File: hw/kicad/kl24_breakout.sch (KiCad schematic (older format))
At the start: 26 parts

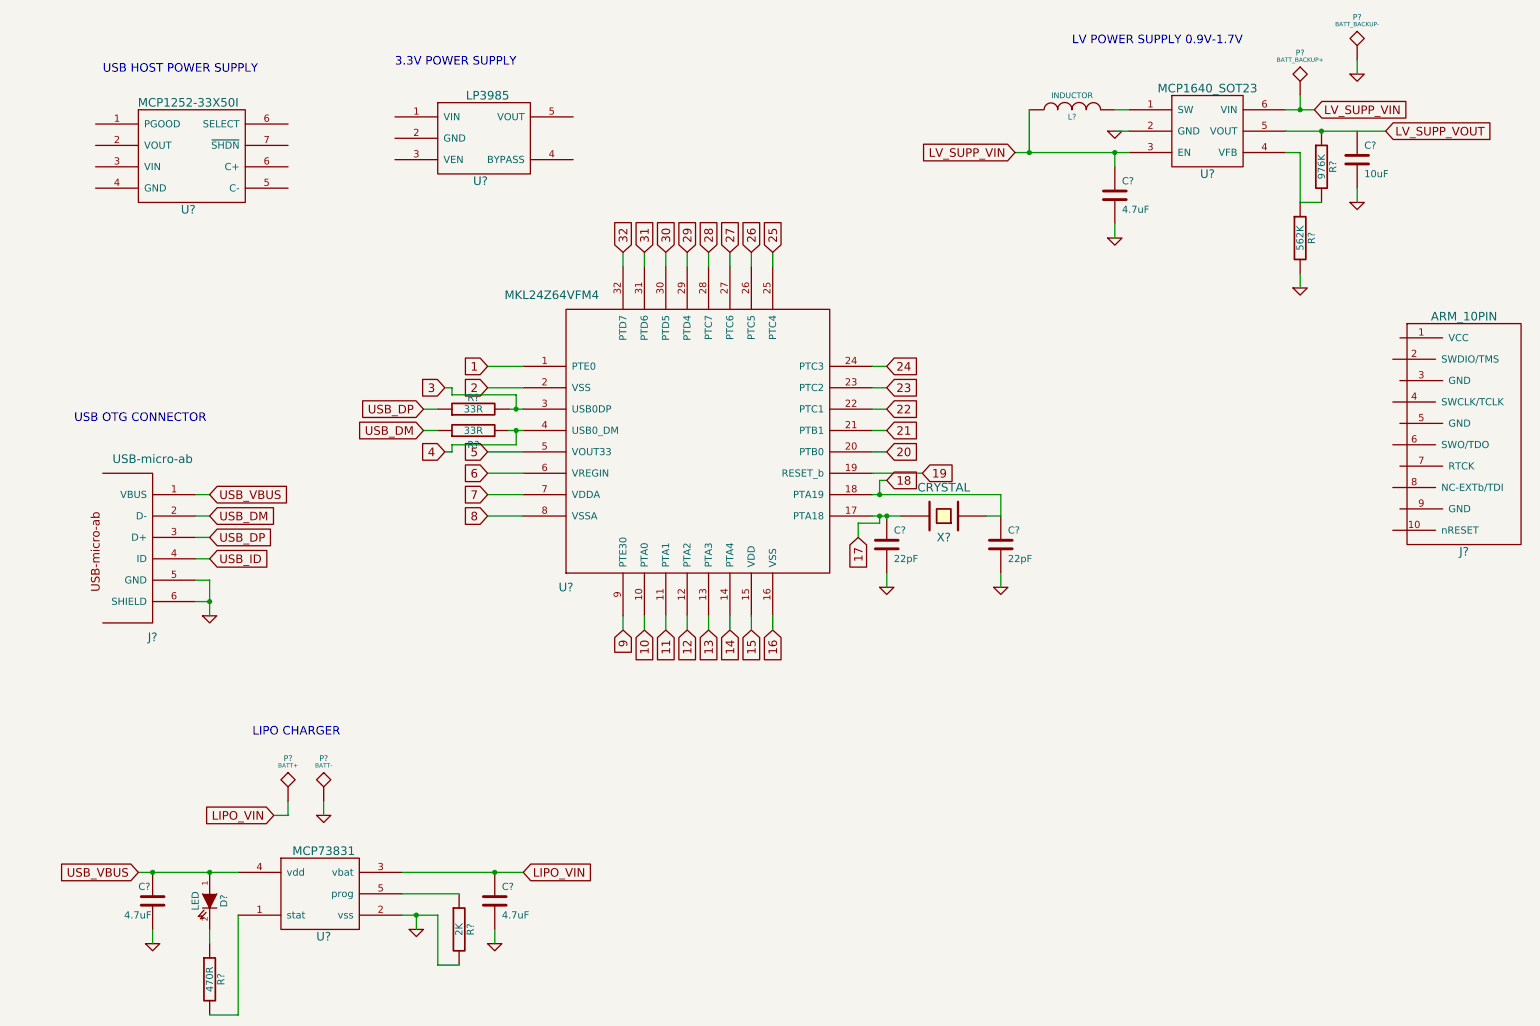
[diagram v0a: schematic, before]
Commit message: - populate 3.3v supply, som rearragning
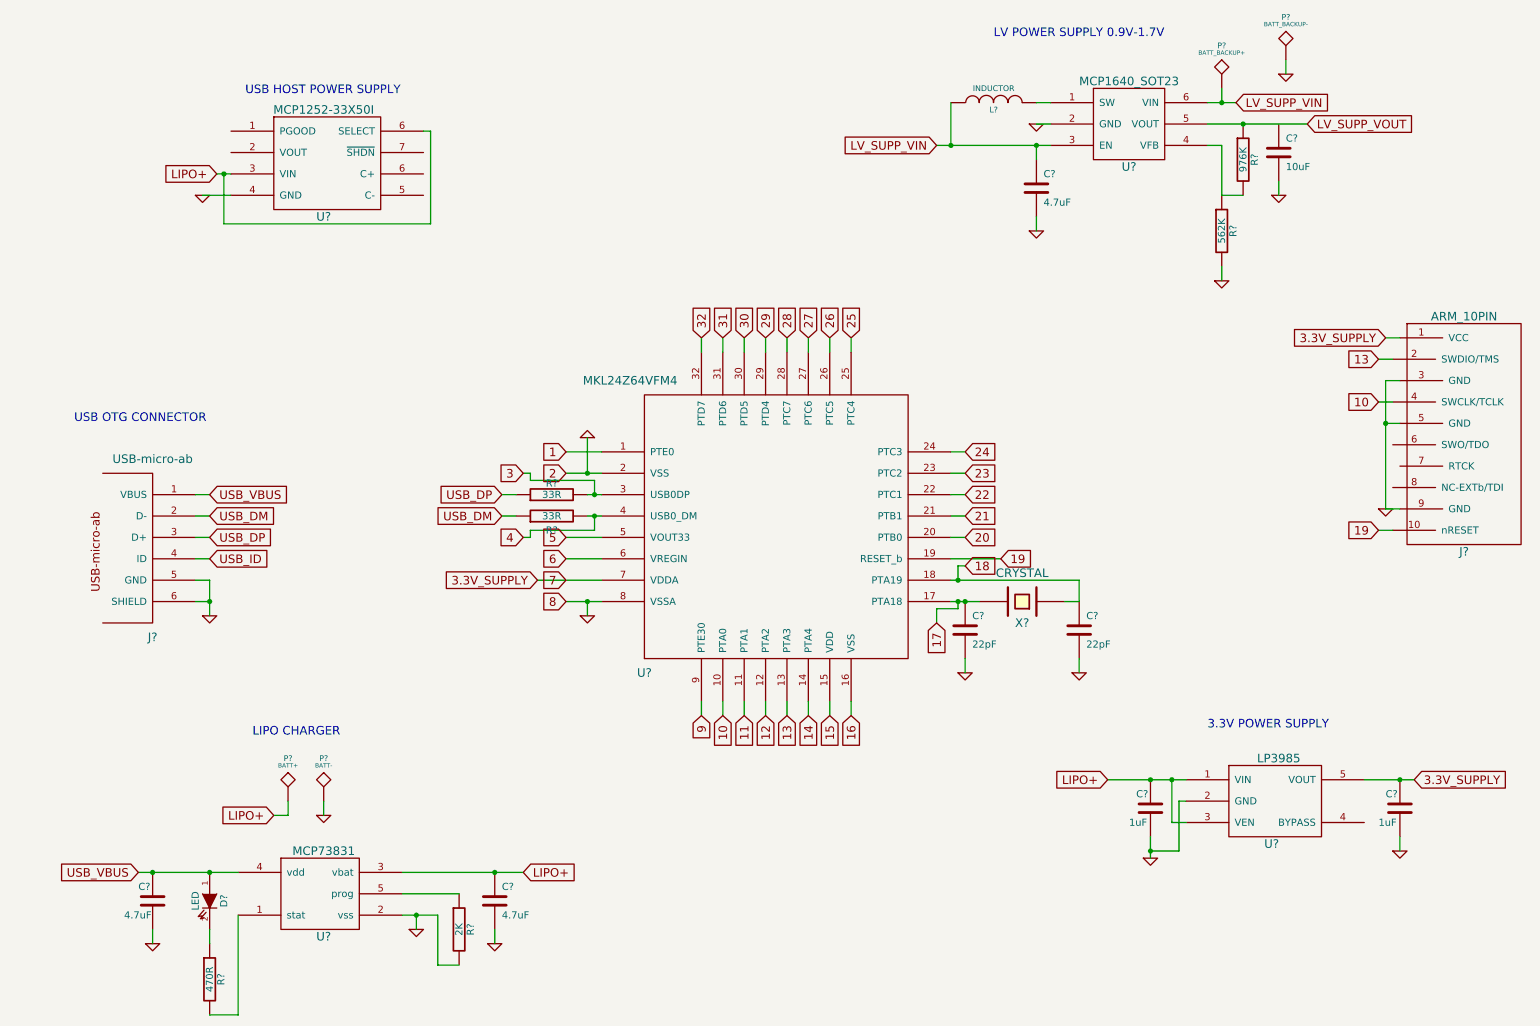
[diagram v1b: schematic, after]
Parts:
- added C? (x2): 1uF, symbol C
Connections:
- net 2 is gone; now on net GND: U?.2 (VSS)
- net 7 is gone; now on net 3.3V_SUPPLY: U?.7 (VDDA)
- net 8 is gone; now on net GND: U?.8 (VSSA)
- net LIPO_VIN is gone; now on net LIPO+: C?.1, P?.1, U?.3 (vbat)
- net 10: now also J?.4 (SWCLK/TCLK)
- net 13: now also J?.2 (SWDIO/TMS)
- net 19: now also J?.10 (nRESET)
- net GND: now also J?.3 (GND), J?.5 (GND), J?.9 (GND), U?.2 (GND), U?.4 (GND), C?.2, C?.2
- net 3.3V_SUPPLY: now reaches J?.1 (VCC)
- net 3.3V_SUPPLY: now also U?.5 (VOUT), C?.1
- net LIPO+: now reaches U?.1 (VIN)
- net LIPO+: now also U?.3 (VEN), U?.3 (VIN), U?.6 (SELECT), C?.1
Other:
- moved on the sheet: C?, L?, P?, R?, U?, X?

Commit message: - fix some erc's - add test points for all micro pins
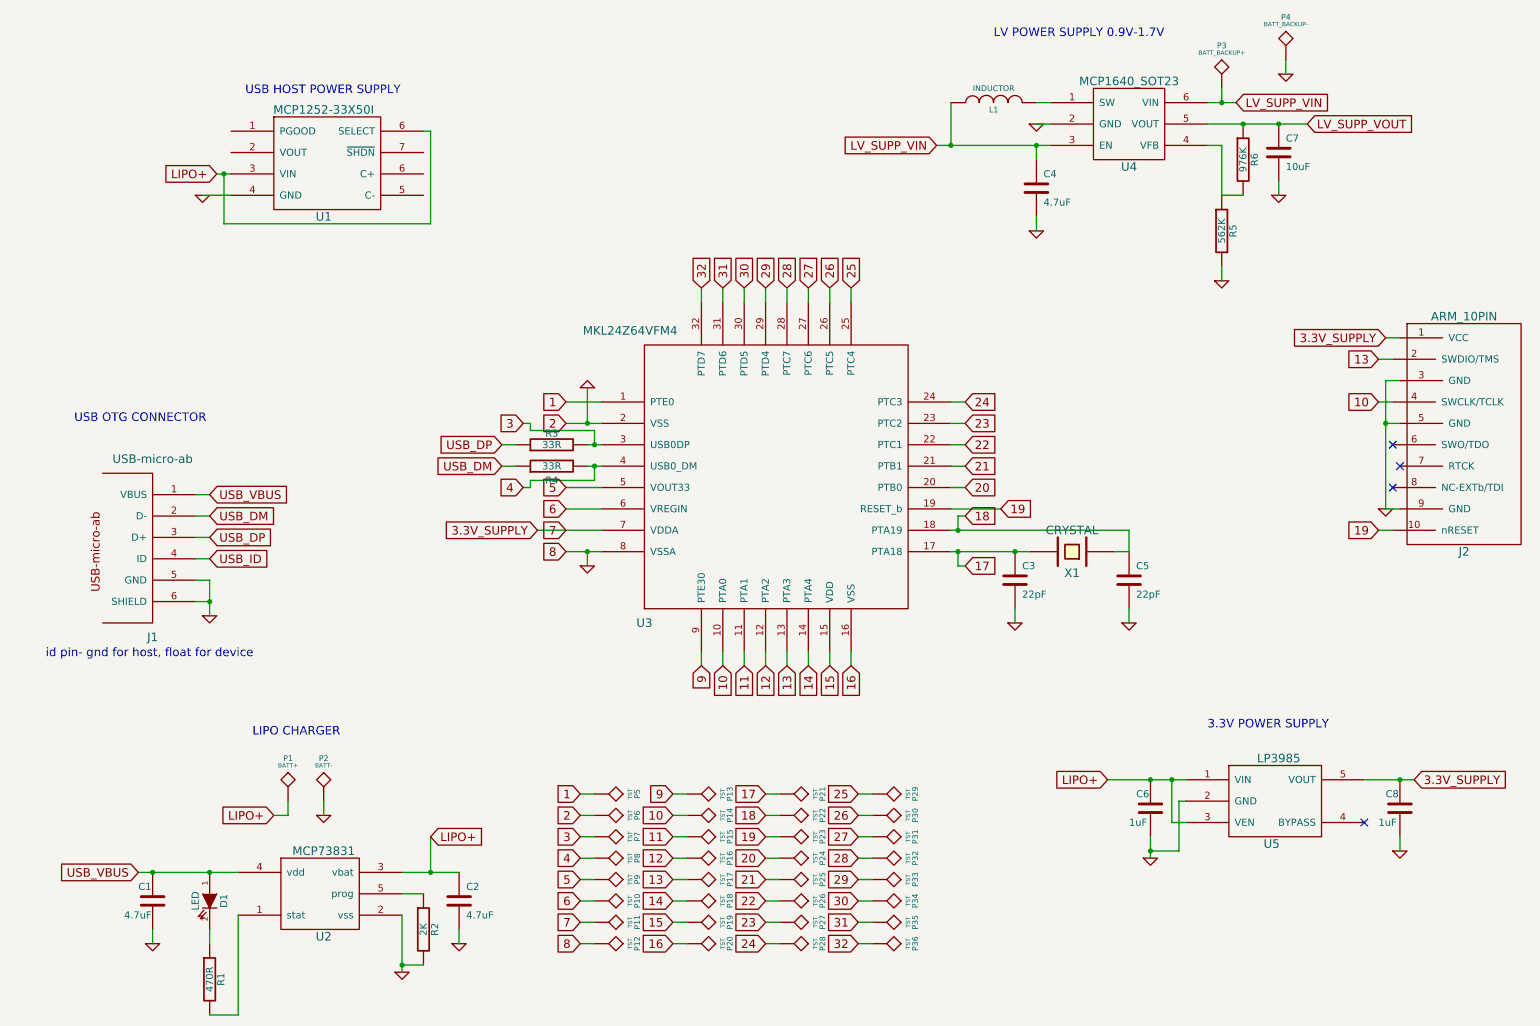
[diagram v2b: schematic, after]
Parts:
- added P10, P11, P12, P13, P14, P15, P16, P17, P18, P19, P20, P21, P22, P23, P24, P25, P26, P27, P28, P29, P30, P31, P32, P33, P34, P35, P36, P5, P6, P7, P8, P9: TST, ~, symbol TST
- gave numbers to parts that had none: 28
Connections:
- net 1: now also P5.1
- net 10: now also P14.1
- net 11: now also P15.1
- net 12: now also P16.1
- net 13: now also P17.1
- net 14: now also P18.1
- net 15: now also P19.1
- net 16: now also P20.1
- net 17: now also P21.1
- net 18: now also P22.1
- net 19: now also P23.1
- net 20: now also P24.1
- net 21: now also P25.1
- net 22: now also P26.1
- net 23: now also P27.1
- net 24: now also P28.1
- net 25: now also P29.1
- net 26: now also P30.1
- net 27: now also P31.1
- net 28: now also P32.1
- net 29: now also P33.1
- net 3: now also P7.1
- net 3.3V_SUPPLY: now also P11.1
- net 30: now also P34.1
- net 31: now also P35.1
- net 32: now also P36.1
- net 4: now also P8.1
- net 5: now also P9.1
- net 6: now also P10.1
- net 9: now also P13.1
- net GND: now also P12.1, P6.1
- net LV_SUPP_VOUT: now also C7.1
- no-connect marks 0 -> 4
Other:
- note added: "id pin- gnd for host, float for device"
- moved on the sheet: C2, C3, C5, R2, R3, R4, U3, X1

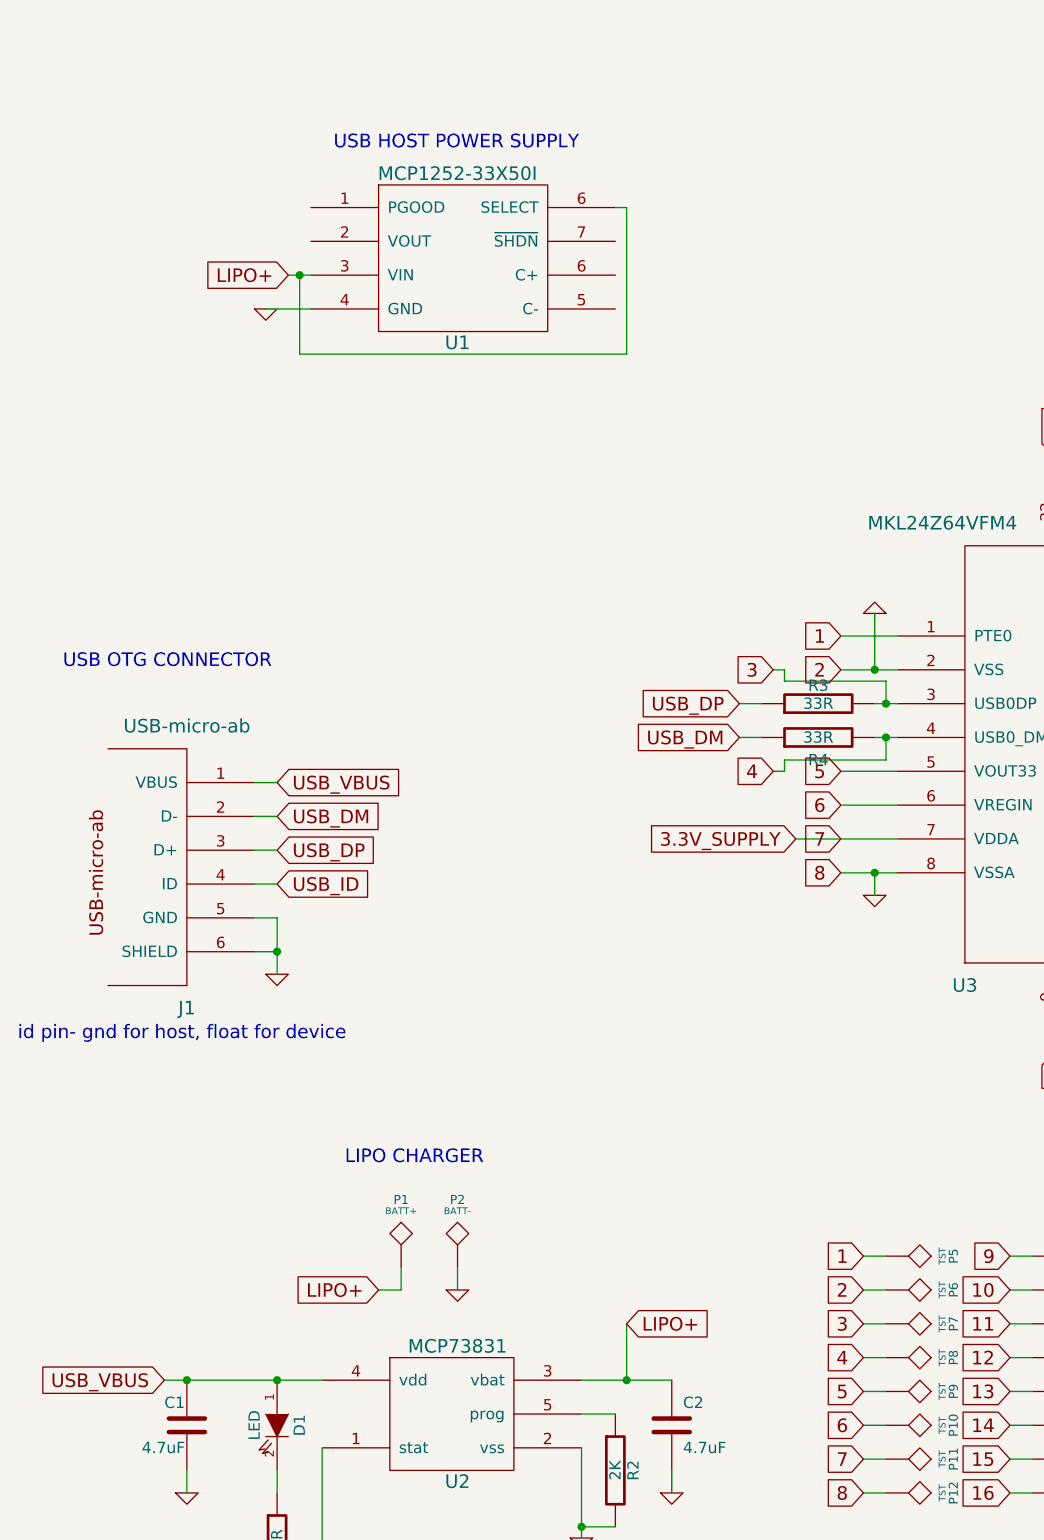
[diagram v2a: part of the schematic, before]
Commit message: - populate 5v boost converter
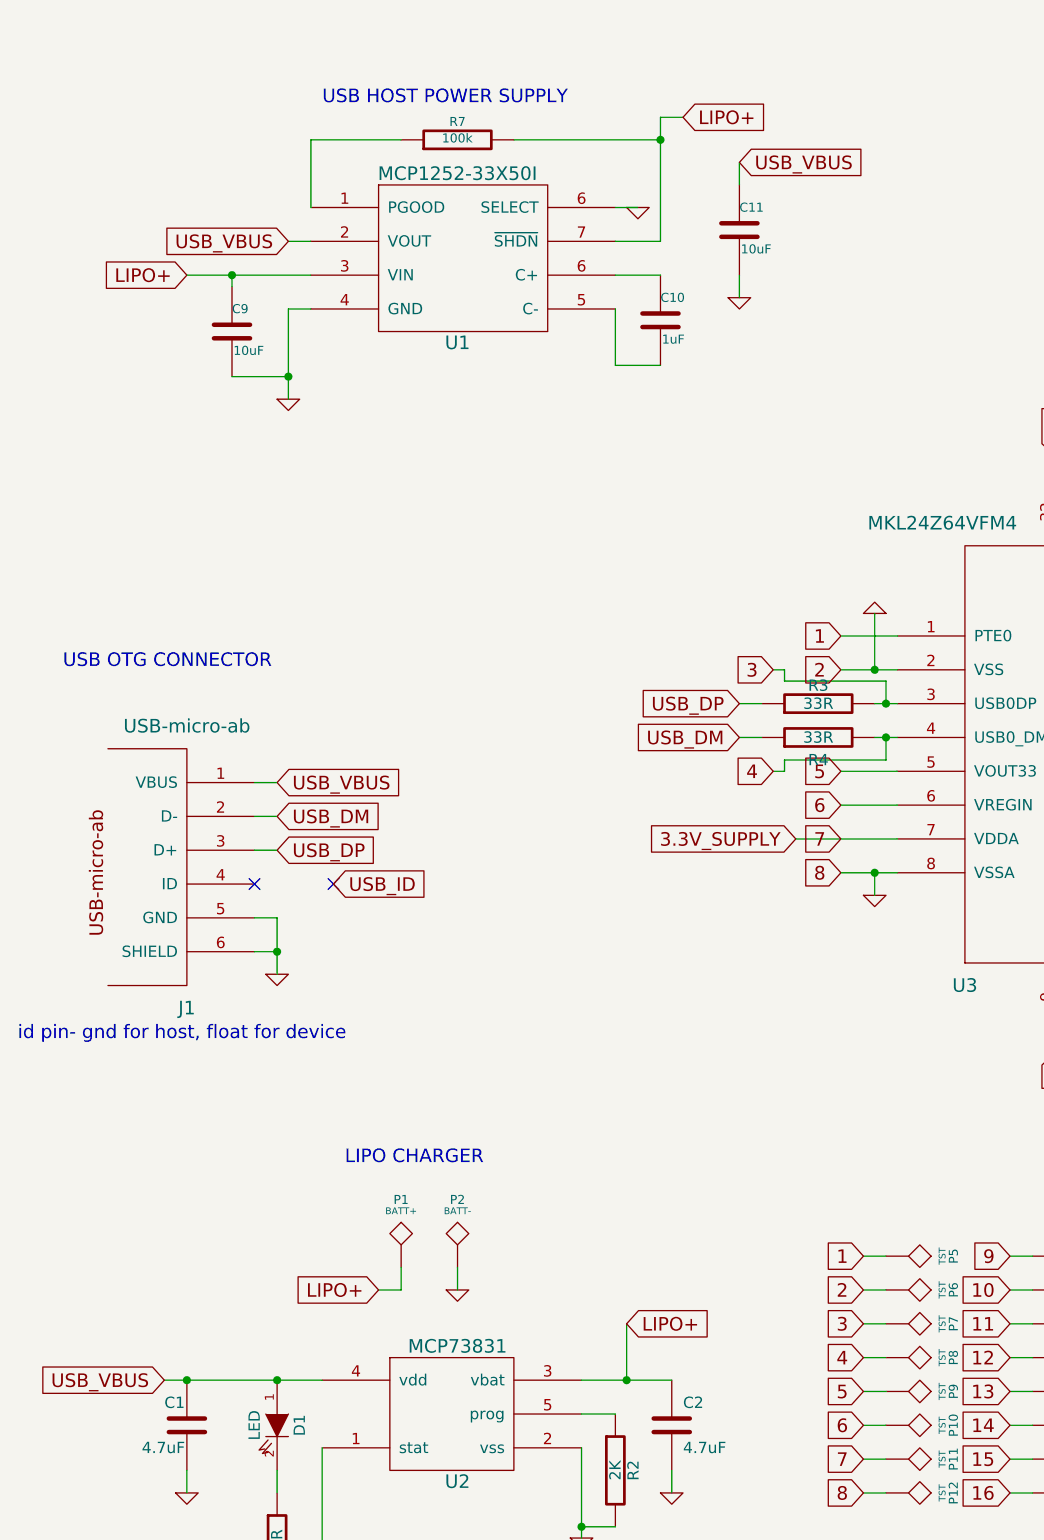
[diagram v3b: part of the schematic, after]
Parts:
- added C10: 1uF, ~, symbol C
- added C11, C9: 10uF, ~, symbol C
- added R7: 100k, ~, symbol R
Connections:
- net GND: now also U1.6 (SELECT), C11.2, C9.2
- net LIPO+: now also U1.7 (~SHDN), C9.1, R7.2; no longer U1.6 (SELECT)
- net USB_ID: no longer J1.4 (ID)
- net USB_VBUS: now also U1.2 (VOUT), C11.1
- net at U1.1 (PGOOD): now also R7.1
- net at U1.5 (C-): now also C10.2
- new net: C10.1, U1.6 (SELECT)
- no-connect marks 4 -> 6
